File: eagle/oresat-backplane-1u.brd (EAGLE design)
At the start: 82.5 x 99 mm, 36 parts, among them J1 5-104196-5, J3 HARWIN-M50-3501042

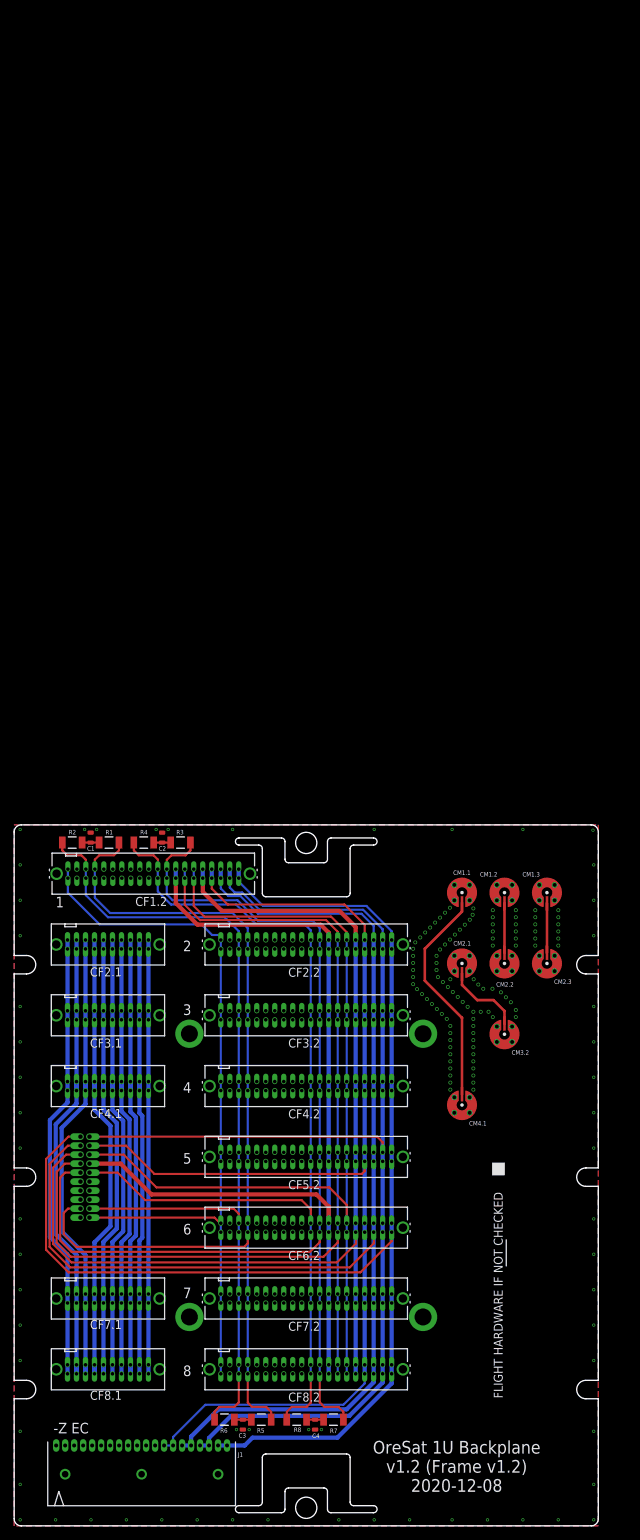
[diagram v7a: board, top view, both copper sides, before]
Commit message: Version 1.3. No significant difference with v1.2 besides added TPLACE block, updated not for flight marker, and fiducials just in case.
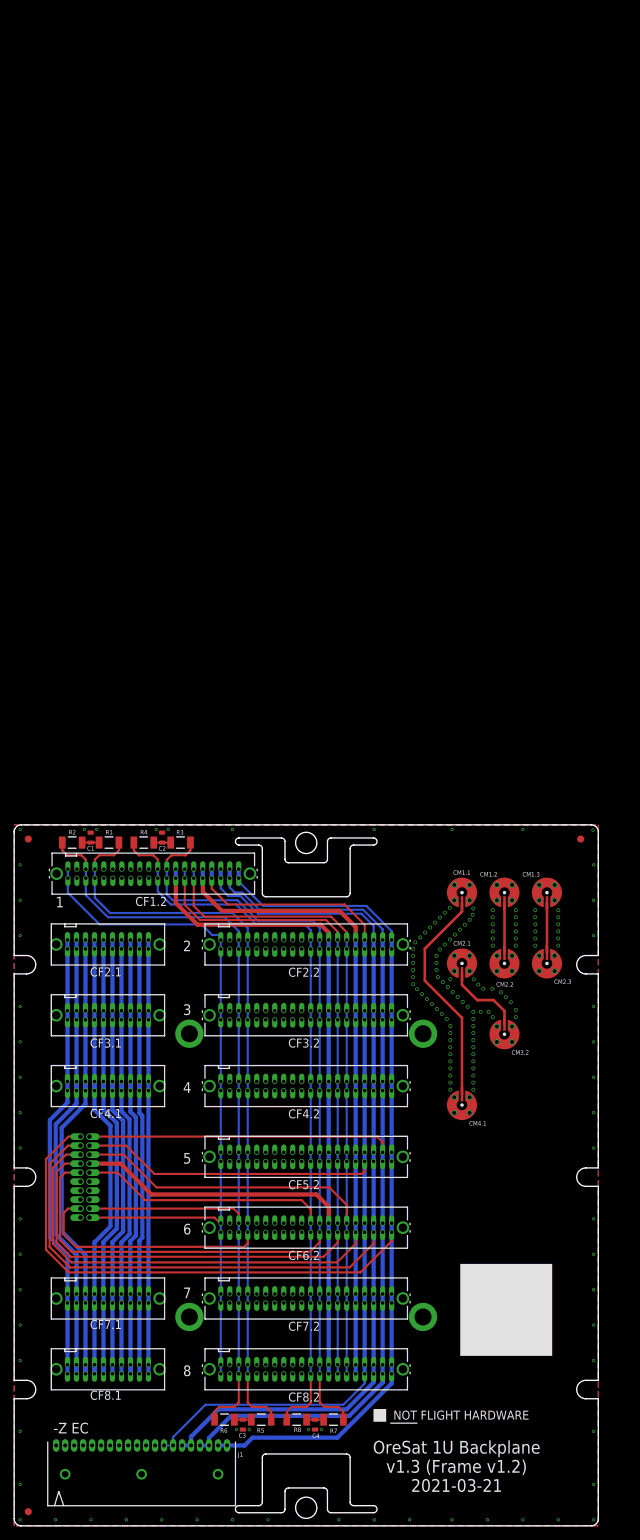
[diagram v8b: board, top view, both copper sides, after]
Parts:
- added FIDUCIAL1, FIDUCIAL2, FIDUCIAL3: FIDUCIAL-1.0X2.0, dock_v2:FIDUCIAL-1.0X2.0
- moved U$1 18.2 mm to (51.0, 15.0), turned to 0 degrees
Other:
- board text added: "OreSat 1U Backplane v1.3 (Frame v1.2) 2021-03-21"
- board text removed: "OreSat 1U Backplane v1.2 (Frame v1.2) 2020-12-08"
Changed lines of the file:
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@@
 <setting verticaltext="up"/>
 </settings>
-<grid distance="0.05" unitdist="mm" unit="mm" style="lines" multiple="1" display="yes" altdistance="0.025" altunitdist="inch" altunit="inch"/>
+<grid distance="1" unitdist="mm" unit="mm" style="lines" multiple="1" display="yes" altdistance="0.025" altunitdist="inch" altunit="inch"/>
 <layers>
-<layer number="1" name="Top" color="4" fill="1" visible="no" active="yes"/>
+<layer number="1" name="Top" color="4" fill="1" visible="yes" active="yes"/>
 <layer number="2" name="Route2" color="7" fill="1" visible="no" active="yes"/>
 <layer number="3" name="Route3" color="4" fill="3" visible="no" active="no"/>
@@
 <layer number="14" name="Route14" color="1" fill="6" visible="no" active="no"/>
 <layer number="15" name="Route15" color="6" fill="1" visible="no" active="yes"/>
-<layer number="16" name="Bottom" color="1" fill="1" visible="yes" active="yes"/>
+<layer number="16" name="Bottom" color="1" fill="1" visible="no" active="yes"/>
 <layer number="17" name="Pads" color="2" fill="1" visible="yes" active="yes"/>
 <layer number="18" name="Vias" color="2" fill="1" visible="yes" active="yes"/>
 <layer number="19" name="Unrouted" color="6" fill="1" visible="yes" active="yes"/>
 <layer number="20" name="Dimension" color="24" fill="1" visible="yes" active="yes"/>
-<layer number="21" name="tPlace" color="7" fill="1" visible="no" active="yes"/>
-<layer number="22" name="bPlace" color="7" fill="1" visible="yes" active="yes"/>
-<layer number="23" name="tOrigins" color="15" fill="1" visible="no" active="yes"/>
-<layer number="24" name="bOrigins" color="15" fill="1" visible="yes" active="yes"/>
-<layer number="25" name="tNames" color="7" fill="1" visible="no" active="yes"/>
+<layer number="21" name="tPlace" color="7" fill="1" visible="yes" active="yes"/>
+<layer number="22" name="bPlace" color="7" fill="1" visible="no" active="yes"/>
+<layer number="23" name="tOrigins" color="15" fill="1" visible="yes" active="yes"/>
+<layer number="24" name="bOrigins" color="15" fill="1" visible="no" active="yes"/>
+<layer number="25" name="tNames" color="7" fill="1" visible="yes" active="yes"/>
 <layer number="26" name="bNames" color="7" fill="1" visible="no" active="yes"/>
 <layer number="27" name="tValues" color="7" fill="1" visible="no" active="yes"/>
 <layer number="28" name="bValues" color="7" fill="1" visible="no" active="yes"/>
-<layer number="29" name="tStop" color="7" fill="3" visible="no" active="yes"/>
+<layer number="29" name="tStop" color="7" fill="3" visible="yes" active="yes"/>
 <layer number="30" name="bStop" color="7" fill="6" visible="no" active="yes"/>
 <layer number="31" name="tCream" color="7" fill="4" visible="no" active="yes"/>
@@
 <layer number="50" name="dxf" color="61" fill="1" visible="no" active="yes"/>
 <layer number="51" name="tDocu" color="7" fill="1" visible="no" active="yes"/>
-<layer number="52" name="bDocu" color="7" fill="1" visible="yes" active="yes"/>
+<layer number="52" name="bDocu" color="7" fill="1" visible="no" active="yes"/>
 <layer number="53" name="tGND_GNDA" color="7" fill="9" visible="no" active="no"/>
 <layer number="54" name="bGND_GNDA" color="1" fill="9" visible="no" active="no"/>
@@
 <layer number="100" name="Muster" color="7" fill="1" visible="no" active="no"/>
 <layer number="101" name="DXF2" color="7" fill="1" visible="no" active="yes"/>
+<layer number="102" name="Changes" color="7" fill="1" visible="no" active="yes"/>
+<layer number="103" name="tMap" color="7" fill="1" visible="no" active="yes"/>
+<layer number="104" name="Name" color="7" fill="1" visible="no" active="yes"/>
+<layer number="105" name="Beschreib" color="7" fill="1" visible="no" active="yes"/>
+<layer number="106" name="BGA-Top" color="7" fill="1" visible="no" active="yes"/>
+<layer number="107" name="BD-Top" color="7" fill="1" visible="no" active="yes"/>
+<layer number="108" name="dxf_notes" color="7" fill="1" visible="no" active="yes"/>
+<layer number="110" name="labels" color="7" fill="1" visible="no" active="yes"/>
+<layer number="111" name="print" color="7" fill="1" visible="no" active="yes"/>
+<layer number="112" name="hints" color="7" fill="1" visible="no" active="yes"/>
+<layer number="116" name="Patch_BOT" color="7" fill="1" visible="no" active="yes"/>
+<layer number="121" name="_tsilk" color="7" fill="1" visible="no" active="yes"/>
+<layer number="122" name="_bsilk" color="7" fill="1" visible="no" active="yes"/>
+<layer number="125" name="_tNames" color="7" fill="1" visible="no" active="yes"/>
+<layer number="144" name="Drill_legend" color="7" fill="1" visible="no" active="yes"/>
+<layer number="151" name="HeatSink" color="7" fill="1" visible="no" active="yes"/>
+<layer number="200" name="200bmp" color="7" fill="1" visible="no" active="yes"/>
+<layer number="201" name="201bmp" color="7" fill="1" visible="no" active="yes"/>
+<layer number="202" name="202bmp" color="7" fill="1" visible="no" active="yes"/>
+<layer number="203" name="203bmp" color="7" fill="1" visible="no" active="yes"/>
+<layer number="204" name="204bmp" color="7" fill="1" visible="no" active="yes"/>
+<layer number="205" name="205bmp" color="7" fill="1" visible="no" active="yes"/>
+<layer number="206" name="206bmp" color="7" fill="1" visible="no" active="yes"/>
+<layer number="207" name="207bmp" color="7" fill="1" visible="no" active="yes"/>
+<layer number="208" name="208bmp" color="7" fill="1" visible="no" active="yes"/>
+<layer number="209" name="209bmp" color="7" fill="1" visible="no" active="yes"/>
+<layer number="210" name="210bmp" color="7" fill="1" visible="no" active="yes"/>
+<layer number="211" name="211bmp" color="7" fill="1" visible="no" active="yes"/>
+<layer number="212" name="212bmp" color="7" fill="1" visible="no" active="yes"/>
+<layer number="213" name="213bmp" color="7" fill="1" visible="no" active="yes"/>
+<layer number="214" name="214bmp" color="7" fill="1" visible="no" active="yes"/>
+<layer number="215" name="215bmp" color="7" fill="1" visible="no" active="yes"/>
+<layer number="216" name="216bmp" color="7" fill="1" visible="no" active="yes"/>
 <layer number="217" name="217bmp" color="18" fill="1" visible="no" active="no"/>
 <layer number="218" name="218bmp" color="19" fill="1" visible="no" active="no"/>
@@
 <layer number="250" name="Descript" color="3" fill="1" visible="no" active="no"/>
 <layer number="251" name="SMDround" color="12" fill="11" visible="no" active="no"/>
+<layer number="254" name="cooling" color="7" fill="1" visible="no" active="yes"/>
 </layers>
 <board>
@@
 <text x="5.55" y="13.05" size="1.5" layer="21" font="vector">-Z EC</text>
 <text x="62.5" y="8.4" size="1.8" layer="21" font="vector" align="center">OreSat 1U Backplane
-v1.2 (Frame v1.2)
-2020-12-08</text>
+v1.3 (Frame v1.2)
+2021-03-21</text>
 <wire x1="75.75" y1="95.25" x2="6.75" y2="95.25" width="0.001" layer="52"/>
 <wire x1="6.75" y1="95.25" x2="4.25" y2="92.75" width="0.001" layer="52" curve="90"/>
@@
 <text x="16.25" y="53.05" size="1.5" layer="22" font="vector" rot="SMR270">DEBUG</text>
 <text x="62.5" y="8.4" size="1.8" layer="22" font="vector" rot="MR0" align="center">OreSat 1U Backplane
-v1.2 (Frame v1.2)
-2020-12-08</text>
+v1.3 (Frame v1.2)
+2021-03-21</text>
 <circle x="10" y="49.25" radius="0.25" width="0.001" layer="50"/>
 <wire x1="9.165" y1="43.335" x2="9.165" y2="55.165" width="0.001" layer="50"/>
@@
 <wire x1="9.165" y1="43.335" x2="10.835" y2="55.165" width="0.001" layer="50"/>
 <wire x1="9.165" y1="55.165" x2="10.835" y2="43.335" width="0.001" layer="50"/>
+<rectangle x1="63" y1="24" x2="76" y2="37" layer="21"/>
 </plain>
 <attributes>
@@
 <attribute name="NAME" x="10.33" y="56.3" size="0.635" layer="26" font="vector" ratio="20" rot="MR0"/>
 </element>
-<element name="U$1" library="oresat-flight-marker" package="FLIGHTMARKER_NEW_BOARDS" value="FLIGHMARKERNEW" x="69" y="18" smashed="yes" rot="R90"/>
+<element name="U$1" library="oresat-flight-marker" package="FLIGHTMARKER_NEW_BOARDS" value="FLIGHMARKERNEW" x="51" y="15" smashed="yes"/>
+<element name="FIDUCIAL1" library="dock_v2" package="FIDUCIAL-1.0X2.0" value="FIDUCIAL-1.0X2.0" x="80" y="97" smashed="yes"/>
+<element name="FIDUCIAL2" library="dock_v2" package="FIDUCIAL-1.0X2.0" value="FIDUCIAL-1.0X2.0" x="2" y="97" smashed="yes"/>
+<element name="FIDUCIAL3" library="dock_v2" package="FIDUCIAL-1.0X2.0" value="FIDUCIAL-1.0X2.0" x="2" y="2" smashed="yes"/>
 </elements>
 <signals>
